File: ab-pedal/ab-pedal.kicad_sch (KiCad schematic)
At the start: 25 parts, among them J1 Barrel_Jack, J2 AudioJack2_Ground_Switch, J3 AudioJack2_Ground_Switch, J4 AudioJack2_Ground_Switch, J5 AudioJack2_Ground_Switch, J6 AudioJack2_Ground_Switch, J7 AudioJack2_Ground_Switch, SW1 TRUE_BYPASS, SW2 INVERT, SW3 INVERT, SW4 ON, U1 TL074, U2 MAX1044

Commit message: started pcb
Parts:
- removed J1: Barrel_Jack, symbol Connector:Barrel_Jack
- added J8: Jack-DC, Connector_PinHeader_2.54mm:PinHeader_1x02_P2.54mm_Vertical, symbol Connector:Jack-DC
- C1, C3: footprint (none) -> Capacitor_THT:C_Rect_L7.2mm_W2.5mm_P5.00mm_FKS2_FKP2_MKS2_MKP2
- C2, C4, C5: footprint (none) -> Capacitor_THT:CP_Radial_D10.0mm_P5.00mm
- D1: footprint (none) -> LED_THT:LED_D5.0mm-4_RGB_Wide_Pins
- J2: value AudioJack2_Ground_Switch -> IN; footprint (none) -> Connector_Audio:Jack_6.35mm_Neutrik_NMJ6HFD2_Horizontal
- J3: value AudioJack2_Ground_Switch -> OUT_A; footprint (none) -> Connector_Audio:Jack_6.35mm_Neutrik_NMJ6HFD2_Horizontal
- J4: value AudioJack2_Ground_Switch -> OUT_B; footprint (none) -> Connector_Audio:Jack_6.35mm_Neutrik_NMJ6HFD2_Horizontal
- J5: value AudioJack2_Ground_Switch -> IN_A; footprint (none) -> Connector_Audio:Jack_6.35mm_Neutrik_NMJ6HFD2_Horizontal
- J6: value AudioJack2_Ground_Switch -> IN_B; footprint (none) -> Connector_Audio:Jack_6.35mm_Neutrik_NMJ6HFD2_Horizontal
- J7: value AudioJack2_Ground_Switch -> OUT; footprint (none) -> Connector_Audio:Jack_6.35mm_Neutrik_NMJ6HFD2_Horizontal
- R1, R2, R3, R4, R5: footprint (none) -> Resistor_THT:R_Axial_DIN0207_L6.3mm_D2.5mm_P10.16mm_Horizontal
- RV1: footprint (none) -> Potentiometer_THT:Potentiometer_Alpha_RD901F-40-00D_Single_Vertical
- SW1, SW2: footprint (none) -> _project:MTS-DPDT
- SW2: renamed from SW3; footprint (none) -> _project:MTS-DPDT
- SW3: renamed from SW4; footprint (none) -> Connector_PinHeader_2.54mm:PinHeader_2x03_P2.54mm_Vertical
- U1: footprint (none) -> Package_DIP:DIP-14_W7.62mm
- U2: footprint (none) -> Package_DIP:DIP-8_W7.62mm
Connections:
- net +9V: now also J8.1
- net GND: now also J8.2
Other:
- note added: "TODO: confirm LEDs"
- note added: "TODO: pot orientation"
- note added: "TODO: switch footprint"
- note added: "TODO: switch orientation"

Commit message: layout
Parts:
- removed J3: OUT_A, Connector_Audio:Jack_6.35mm_Neutrik_NMJ6HFD2_Horizontal, symbol Connector_Audio:AudioJack2_Ground_Switch
- removed J5: IN_A, Connector_Audio:Jack_6.35mm_Neutrik_NMJ6HFD2_Horizontal, symbol Connector_Audio:AudioJack2_Ground_Switch
- added J1: PEDAL, Connector_Audio:Jack_6.35mm_Neutrik_NMJ6HFD2_Horizontal, symbol Connector_Audio:AudioJack3_Switch
- C2, C4, C5: footprint Capacitor_THT:CP_Radial_D10.0mm_P5.00mm -> Capacitor_THT:CP_Radial_D4.0mm_P2.00mm
- J2, J7: symbol Connector_Audio:AudioJack2_Ground_Switch -> Connector_Audio:AudioJack3_Switch
- J4: value OUT_B -> SEND; symbol Connector_Audio:AudioJack2_Ground_Switch -> Connector_Audio:AudioJack3_Switch
- J6: value IN_B -> RECV; symbol Connector_Audio:AudioJack2_Ground_Switch -> Connector_Audio:AudioJack3_Switch
- R1, R2, R3, R4, R5: footprint Resistor_THT:R_Axial_DIN0207_L6.3mm_D2.5mm_P10.16mm_Horizontal -> Resistor_THT:R_Axial_DIN0207_L6.3mm_D2.5mm_P5.08mm_Vertical
- SW3: footprint Connector_PinHeader_2.54mm:PinHeader_2x03_P2.54mm_Vertical -> _project:PinHeader_2x03_P2.54mm_Vertical
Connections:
- net BLEND: now also SW3.6 (C), U1.7; no longer SW3.1 (A), U1.8
- net GND: now also J2.R, J2.RN, J4.R, J4.RN, J6.R, J6.RN, J7.R, J7.RN, SW3.2 (B), U1.12 (+); no longer J2.G, J4.G, J6.G, J7.G, J7.TN, SW3.5 (B), U1.10 (+)
- net IN: now also SW1.6 (C), U1.10 (+); no longer SW1.3 (C), U1.3 (+)
- net OUT: now also SW1.2 (B); no longer SW1.5 (B)
- net at D1.2 (RK): now also SW3.1 (A); no longer SW3.4 (A)
- net at D1.3 (GK): now also SW3.3 (C); no longer SW3.6 (C)
- net at SW2.4 (A): now also SW2.1 (A); no longer R1.1
- net at SW2.6 (C): now also R1.1; no longer SW2.3 (C)
- net at R3.1: now also J1.R; no longer RV1.2
- net at R1.2, R2.1: now also U1.13 (-); no longer U1.6 (-)
- net at R3.2, R4.1: now also U1.6 (-); no longer U1.9 (-)
- net IN_A: no longer names the net of SW1.1 (A)
- net IN_A: now also U1.1, U1.2 (-); no longer RV1.1
- net IN_B renamed RETURN
- net IN_B~: no longer names the net of RV1.3
- net IN_B~: now also J1.TN; no longer SW2.2 (B)
- removed net OUT_A: J4.T, U1.1, U1.2 (-)
- new net: SW1.3 (C), SW3.5 (B), U1.3 (+)
- new net: J1.RN, RV1.2
- new net: J1.SN, RV1.1
- new net: SW1.5 (B), SW3.4 (A)
- new net: R2.2, SW2.3 (C), U1.14
- new net BUFFERED: J1.T, J4.T, SW1.4 (A), U1.8, U1.9 (-)
- new net RETURN~: J1.S, SW2.2 (B)
- no-connect marks 3 -> 4
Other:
- moved on the sheet: R1, R2, R3, R4, RV1, SW1A, SW1B, SW2A, SW2B, SW3A, SW3B, U1A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

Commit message: update for mechanicals
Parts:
- D1: symbol Device:LED_ARGB -> Device:LED_BGAR
- J1, J2, J4, J6, J7: footprint Connector_Audio:Jack_6.35mm_Neutrik_NMJ6HFD2_Horizontal -> _project:Jack_6.35mm_Neutrik_NMJ6HCD3_Horizontal
- R5: value 1k -> 10k
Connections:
- net at D1.1 (BK): now also SW3.3 (C); no longer R5.2
- net at D1.2 (GK): no longer SW3.1 (A)
- net at D1.3 (A): now also R5.2; no longer SW3.3 (C)
- net at D1.4 (RK): now also SW3.1 (A)
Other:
- note removed: "TODO: confirm LEDs"
- note removed: "TODO: pot orientation"
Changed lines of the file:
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@@
 		)
 	)
-	(text "TODO: pot orientation"
-		(exclude_from_sim no)
-		(at 186.69 77.724 0)
-		(effects
-			(font
-				(size 1.27 1.27)
-			)
-		)
-	)
 	(text "bypass"
 		(exclude_from_sim no)
@@
 		)
 	)
-	(text "TODO: confirm LEDs"
-		(exclude_from_sim no)
-		(at 227.076 35.306 0)
-		(effects
-			(font
-				(size 1.27 1.27)
-			)
-		)
-	)
 	(text "RED or GREEN indicates state"
 		(exclude_from_sim no)
@@
 	)
 	(no_connect
-		(at 220.98 45.72)
+		(at 215.9 45.72)
 	)
 	(no_connect
@@
 	(wire
 		(pts
-			(xy 215.9 45.72) (xy 215.9 50.8)
+			(xy 204.47 119.38) (xy 207.01 119.38)
 		)
 		(stroke
@@
 	(wire
 		(pts
-			(xy 204.47 119.38) (xy 207.01 119.38)
+			(xy 210.82 45.72) (xy 210.82 50.8)
 		)
 		(stroke
@@
 	(wire
 		(pts
-			(xy 210.82 45.72) (xy 210.82 50.8)
-		)
-		(stroke
-			(width 0)
-			(type default)
-		)
-	)
-	(wire
-		(pts
 			(xy 148.59 128.27) (xy 151.13 128.27)
 		)
@@
 	(wire
 		(pts
+			(xy 215.9 50.8) (xy 220.98 50.8)
+		)
+		(stroke
+			(width 0)
+			(type default)
+		)
+	)
+	(wire
+		(pts
 			(xy 171.45 137.16) (xy 171.45 128.27)
 		)
@@
 	(wire
 		(pts
+			(xy 220.98 50.8) (xy 220.98 45.72)
+		)
+		(stroke
+			(width 0)
+			(type default)
+		)
+	)
+	(wire
+		(pts
 			(xy 153.67 105.41) (xy 156.21 105.41)
 		)
@@
 			)
 		)
-		(property "Footprint" "Connector_Audio:Jack_6.35mm_Neutrik_NMJ6HFD2_Horizontal"
+		(property "Footprint" "_project:Jack_6.35mm_Neutrik_NMJ6HCD3_Horizontal"
 			(at 85.09 116.84 0)
 			(effects
@@
 	)
 	(symbol
-		(lib_id "Device:LED_ARGB")
+		(lib_id "Device:LED_BGAR")
 		(at 215.9 40.64 90)
 		(unit 1)
@@
 			)
 		)
-		(property "Description" "RGB LED, anode/red/green/blue"
+		(property "Description" "RGB LED, blue/green/anode/red"
 			(at 215.9 40.64 0)
 			(effects
@@
 			)
 		)
-		(property "Footprint" "Connector_Audio:Jack_6.35mm_Neutrik_NMJ6HFD2_Horizontal"
+		(property "Footprint" "_project:Jack_6.35mm_Neutrik_NMJ6HCD3_Horizontal"
 			(at 22.86 102.87 0)
 			(effects
@@
 			)
 		)
-		(property "Footprint" "Connector_Audio:Jack_6.35mm_Neutrik_NMJ6HFD2_Horizontal"
+		(property "Footprint" "_project:Jack_6.35mm_Neutrik_NMJ6HCD3_Horizontal"
 			(at 167.64 62.23 0)
 			(effects
@@
 			)
 		)
-		(property "Footprint" "Connector_Audio:Jack_6.35mm_Neutrik_NMJ6HFD2_Horizontal"
+		(property "Footprint" "_project:Jack_6.35mm_Neutrik_NMJ6HCD3_Horizontal"
 			(at 271.78 129.54 0)
 			(effects
@@
 			)
 		)
-		(property "Value" "1k"
+		(property "Value" "10k"
 			(at 218.44 30.4799 0)
 			(effects
@@
 			)
 		)
-		(property "Footprint" "Connector_Audio:Jack_6.35mm_Neutrik_NMJ6HFD2_Horizontal"
+		(property "Footprint" "_project:Jack_6.35mm_Neutrik_NMJ6HCD3_Horizontal"
 			(at 71.12 116.84 0)
 			(effects

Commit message: update layout
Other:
- note added: "RED or BLUE indicates state"
- note removed: "RED or GREEN indicates state"
- note removed: "TODO: switch footprint"
- note removed: "TODO: switch orientation"
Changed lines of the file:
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@@
 	(generator_version "9.0")
 	(paper "A4")
-	(text "TODO: switch orientation"
-		(exclude_from_sim no)
-		(at 251.968 94.488 0)
-		(effects
-			(font
-				(size 1.27 1.27)
-			)
-		)
-	)
-	(text "TODO: switch orientation"
-		(exclude_from_sim no)
-		(at 139.446 118.872 0)
-		(effects
-			(font
-				(size 1.27 1.27)
-			)
-		)
-	)
 	(text "Negative supply charge pump\nconnecting boost to VCC increases\nswtiching frequency to avoid audio interference"
 		(exclude_from_sim no)
@@
 		)
 	)
-	(text "TODO: switch footprint"
-		(exclude_from_sim no)
-		(at 256.032 113.792 0)
-		(effects
-			(font
-				(size 1.27 1.27)
-			)
-		)
-	)
-	(text "RED or GREEN indicates state"
+	(text "RED or BLUE indicates state"
 		(exclude_from_sim no)
 		(at 204.216 37.084 90)
 		(effects
 			(font
-				(size 1.27 1.27)
-			)
-		)
-	)
-	(text "TODO: switch footprint"
-		(exclude_from_sim no)
-		(at 124.46 143.764 0)
-		(effects
-			(font

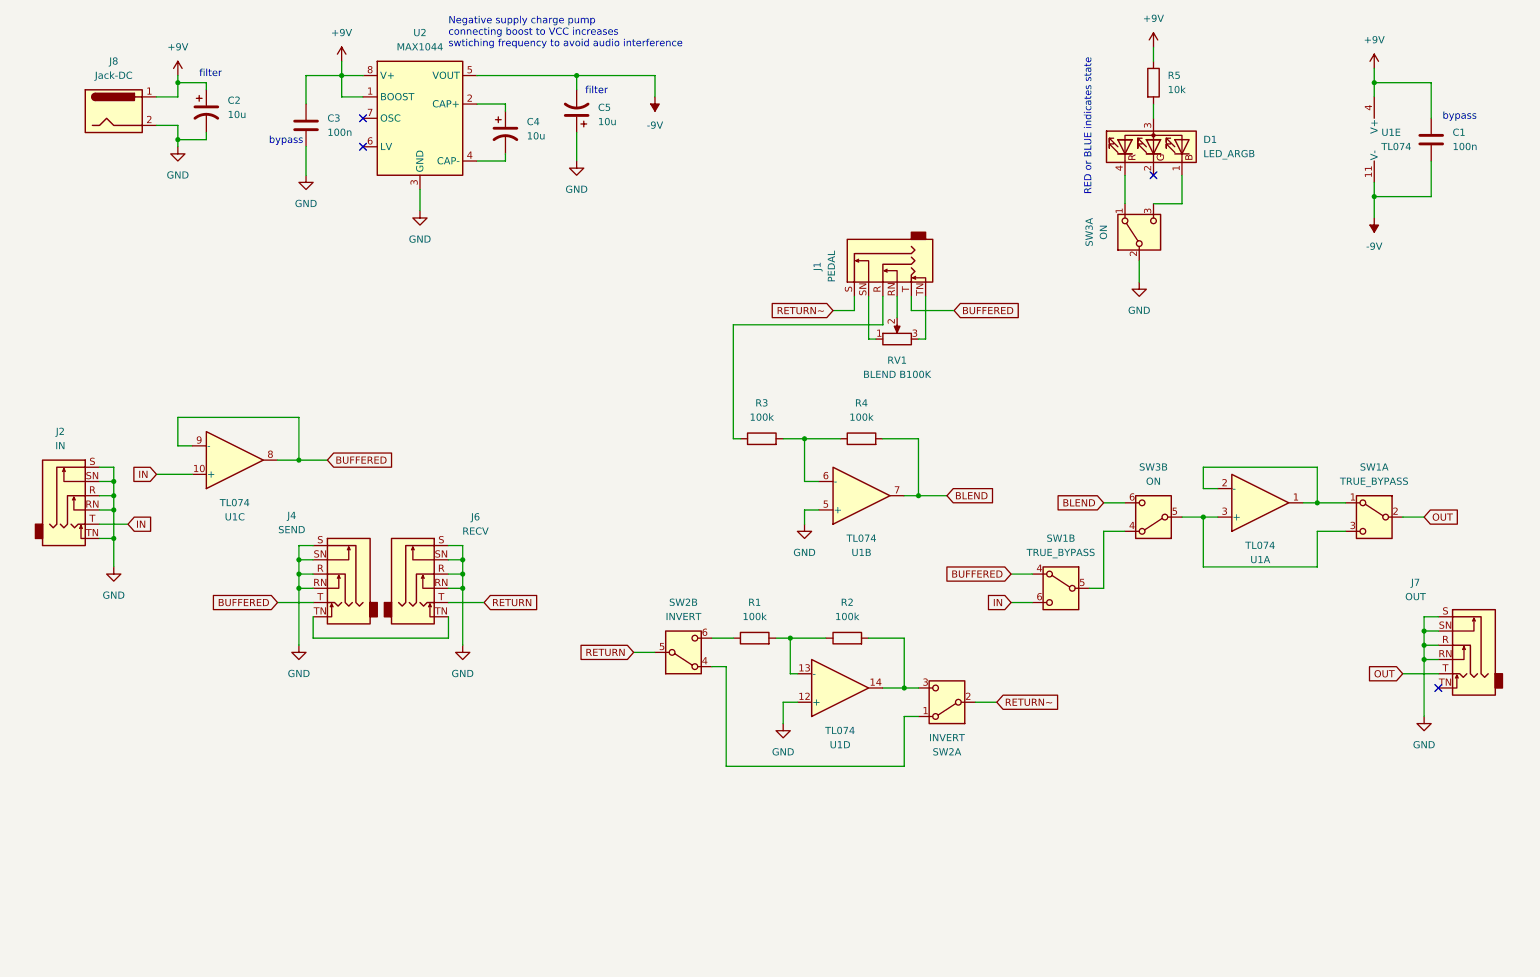
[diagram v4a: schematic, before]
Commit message: add regulators
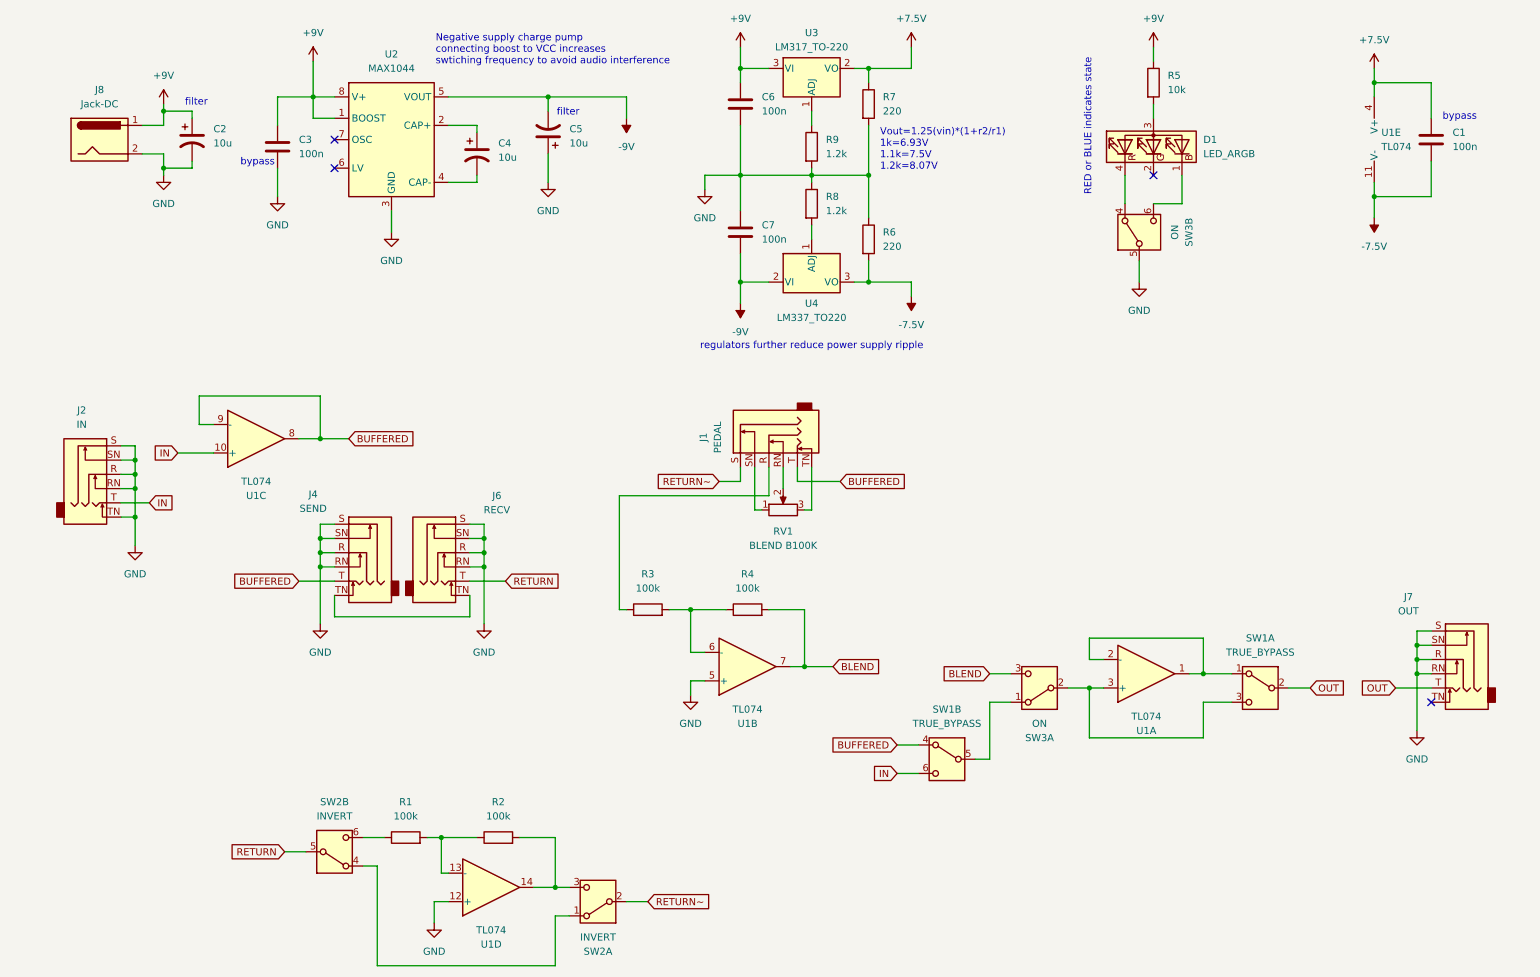
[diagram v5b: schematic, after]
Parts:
- added C6, C7: 100n, Capacitor_THT:C_Rect_L7.2mm_W2.5mm_P5.00mm_FKS2_FKP2_MKS2_MKP2, symbol Device:C
- added R6, R7: 220, Resistor_THT:R_Axial_DIN0207_L6.3mm_D2.5mm_P5.08mm_Vertical, symbol Device:R
- added R8, R9: 1.2k, Resistor_THT:R_Axial_DIN0207_L6.3mm_D2.5mm_P5.08mm_Vertical, symbol Device:R
- added U3: LM317_TO-220, Package_TO_SOT_THT:TO-220-3_Vertical, symbol Regulator_Linear:LM317_TO-220
- added U4: LM337_TO220, Package_TO_SOT_THT:TO-220-3_Vertical, symbol Regulator_Linear:LM337_TO220
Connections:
- net +9V: now also C6.1, U3.3 (VI); no longer C1.1, U1.4 (V+)
- net -9V: now also C7.2, U4.2 (VI); no longer C1.2, U1.11 (V-)
- net BLEND: now also SW3.3 (C); no longer SW3.6 (C)
- net GND: now also SW3.5 (B), C6.2, C7.1, R6.1, R7.2, R8.1, R9.2; no longer SW3.2 (B)
- net at D1.1 (BK): now also SW3.6 (C); no longer SW3.3 (C)
- net at D1.4 (RK): now also SW3.4 (A); no longer SW3.1 (A)
- net at SW1.3 (C), U1.3 (+): now also SW3.2 (B); no longer SW3.5 (B)
- net at SW1.5 (B): now also SW3.1 (A); no longer SW3.4 (A)
- new net: R8.2, U4.1 (ADJ)
- new net: R9.1, U3.1 (ADJ)
- new net +7.5V: C1.1, R7.1, U1.4 (V+), U3.2 (VO)
- new net -7.5V: C1.2, R6.2, U1.11 (V-), U4.3 (VO)
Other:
- note added: "Vout=1.25(vin)*(1+r2/r1) 1k=6.93V 1.1k=7.5V 1.2k=8.07V"
- note added: "regulators further reduce power supply ripple"
- moved on the sheet: C2, C3, C4, C5, J1, J2, J4, J6, J7, J8, R1, R2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

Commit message: optimize nets
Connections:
- net BUFFERED: now also SW1.1 (A), U1.1, U1.2 (-); no longer SW1.4 (A), U1.8, U1.9 (-)
- net IN: now also SW1.3 (C), U1.3 (+); no longer SW1.6 (C), U1.10 (+)
- net OUT: now also SW1.5 (B); no longer SW1.2 (B)
- net at SW3.1 (A): now also SW1.2 (B); no longer SW1.5 (B)
- new net: SW1.6 (C), SW3.2 (B), U1.10 (+)
- new net: SW1.4 (A), U1.8, U1.9 (-)
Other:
- moved on the sheet: SW1A, SW1B, U1A, U1C
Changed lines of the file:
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@@
 	(symbol
 		(lib_id "Switch:SW_DPDT_x2")
-		(at 234.95 137.16 0)
+		(at 179.07 149.86 0)
 		(mirror y)
 		(unit 1)
@@
 		(dnp no)
 		(property "Reference" "SW1"
-			(at 234.95 128.27 0)
+			(at 179.07 140.97 0)
 			(effects
 				(font
@@
 		)
 		(property "Value" "TRUE_BYPASS"
-			(at 234.95 130.81 0)
+			(at 179.07 143.51 0)
 			(effects
 				(font
@@
 		)
 		(property "Footprint" "_project:MTS-DPDT"
-			(at 234.95 137.16 0)
+			(at 179.07 149.86 0)
 			(effects
 				(font
@@
 		)
 		(property "Datasheet" "~"
-			(at 234.95 137.16 0)
+			(at 179.07 149.86 0)
 			(effects
 				(font
@@
 		)
 		(property "Description" "Switch, dual pole double throw, separate symbols"
-			(at 234.95 137.16 0)
+			(at 179.07 149.86 0)
 			(effects
 				(font
@@
 	(symbol
 		(lib_id "Amplifier_Operational:TL074")
-		(at 55.88 92.71 0)
+		(at 214.63 134.62 0)
 		(mirror x)
 		(unit 3)
@@
 		(dnp no)
 		(property "Reference" "U1"
-			(at 55.88 102.87 0)
+			(at 214.63 144.78 0)
 			(effects
 				(font
@@
 		)
 		(property "Value" "TL074"
-			(at 55.88 100.33 0)
+			(at 214.63 142.24 0)
 			(effects
 				(font
@@
 		)
 		(property "Footprint" "Package_DIP:DIP-14_W7.62mm"
-			(at 54.61 95.25 0)
+			(at 213.36 137.16 0)
 			(effects
 				(font
@@
 		)
 		(property "Datasheet" "http://www.ti.com/lit/ds/symlink/tl071.pdf"
-			(at 57.15 97.79 0)
+			(at 215.9 139.7 0)
 			(effects
 				(font
@@
 		)
 		(property "Description" "Quad Low-Noise JFET-Input Operational Amplifiers, DIP-14/SOIC-14"
-			(at 55.88 92.71 0)
+			(at 214.63 134.62 0)
 			(effects
 				(font
@@
 	(symbol
 		(lib_id "Switch:SW_DPDT_x2")
-		(at 179.07 149.86 0)
+		(at 234.95 137.16 0)
 		(mirror y)
 		(unit 2)
@@
 		(dnp no)
 		(property "Reference" "SW1"
-			(at 179.07 140.97 0)
+			(at 234.95 128.27 0)
 			(effects
 				(font
@@
 		)
 		(property "Value" "TRUE_BYPASS"
-			(at 179.07 143.51 0)
+			(at 234.95 130.81 0)
 			(effects
 				(font
@@
 		)
 		(property "Footprint" "_project:MTS-DPDT"
-			(at 179.07 149.86 0)
+			(at 234.95 137.16 0)
 			(effects
 				(font
@@
 		)
 		(property "Datasheet" "~"
-			(at 179.07 149.86 0)
+			(at 234.95 137.16 0)
 			(effects
 				(font
@@
 		)
 		(property "Description" "Switch, dual pole double throw, separate symbols"
-			(at 179.07 149.86 0)
+			(at 234.95 137.16 0)
 			(effects
 				(font
@@
 	(symbol
 		(lib_id "Amplifier_Operational:TL074")
-		(at 214.63 134.62 0)
+		(at 55.88 92.71 0)
 		(mirror x)
 		(unit 1)
@@
 		(dnp no)
 		(property "Reference" "U1"
-			(at 214.63 144.78 0)
+			(at 55.88 102.87 0)
 			(effects
 				(font
@@
 		)
 		(property "Value" "TL074"
-			(at 214.63 142.24 0)
+			(at 55.88 100.33 0)
 			(effects
 				(font
@@
 		)
 		(property "Footprint" "Package_DIP:DIP-14_W7.62mm"
-			(at 213.36 137.16 0)
+			(at 54.61 95.25 0)
 			(effects
 				(font
@@
 		)
 		(property "Datasheet" "http://www.ti.com/lit/ds/symlink/tl071.pdf"
-			(at 215.9 139.7 0)
+			(at 57.15 97.79 0)
 			(effects
 				(font
@@
 		)
 		(property "Description" "Quad Low-Noise JFET-Input Operational Amplifiers, DIP-14/SOIC-14"
-			(at 214.63 134.62 0)
-			(effects
-				(font
+			(at 55.88 92.71 0)
+			(effects
+				(font
